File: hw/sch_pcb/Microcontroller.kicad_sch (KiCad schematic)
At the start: 32 parts

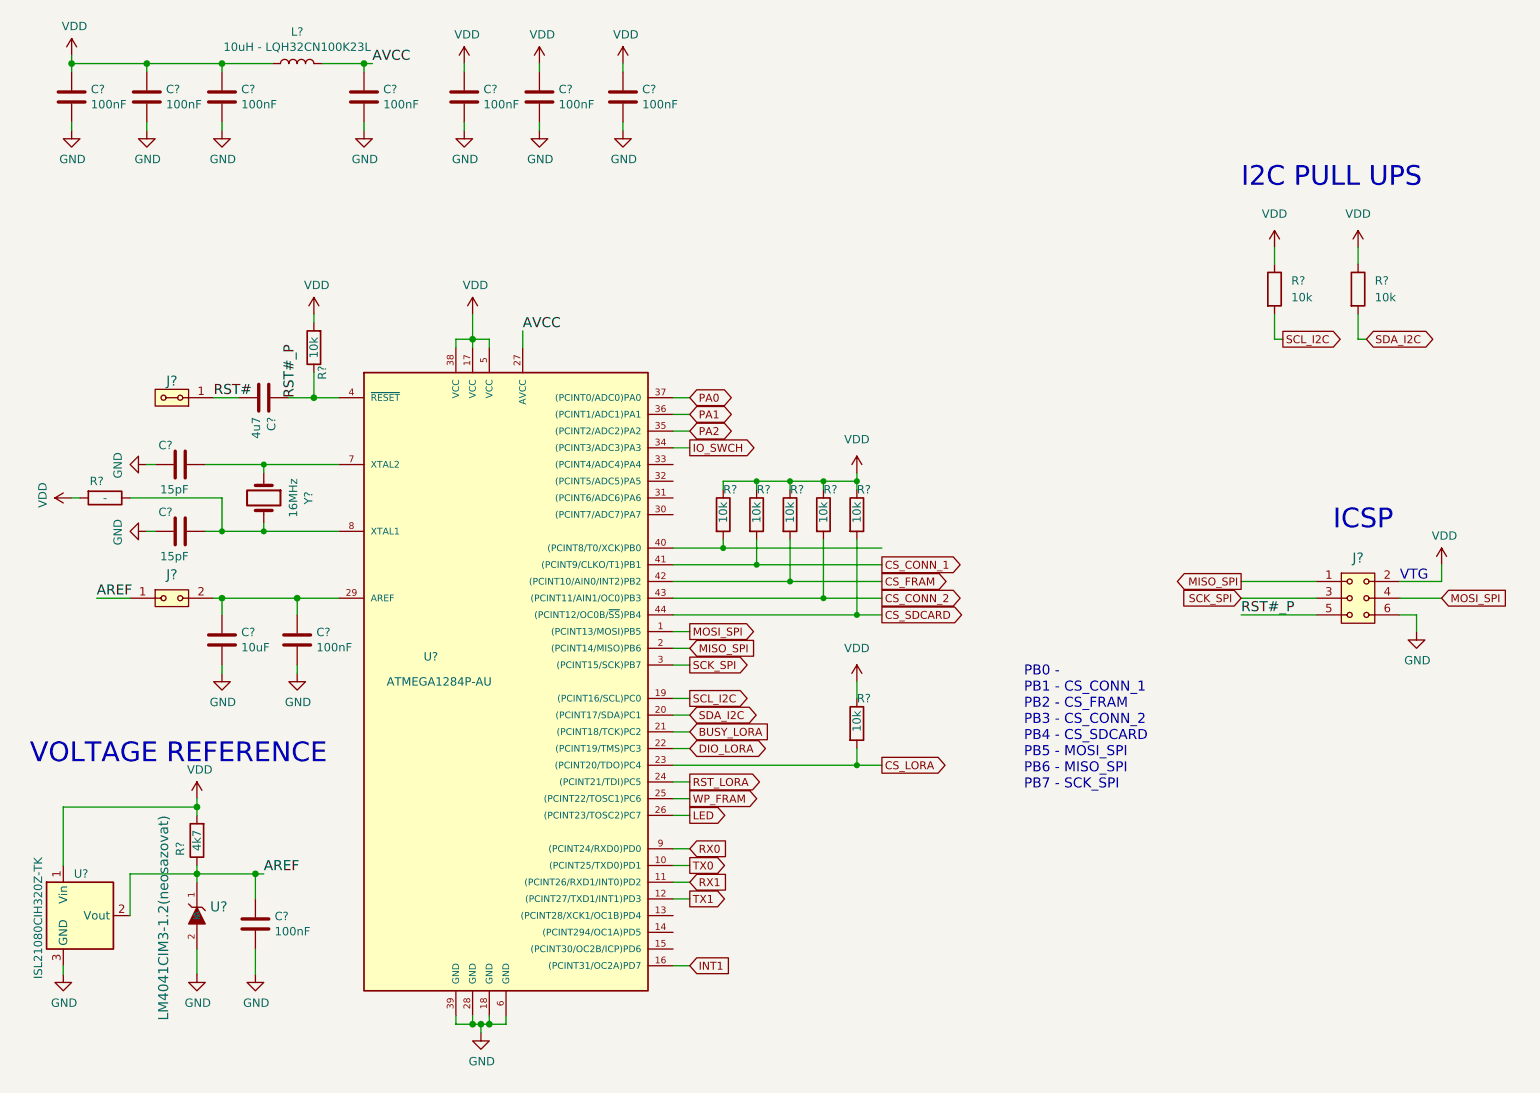
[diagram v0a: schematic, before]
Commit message: schematics update - LTC4041, TPS631000
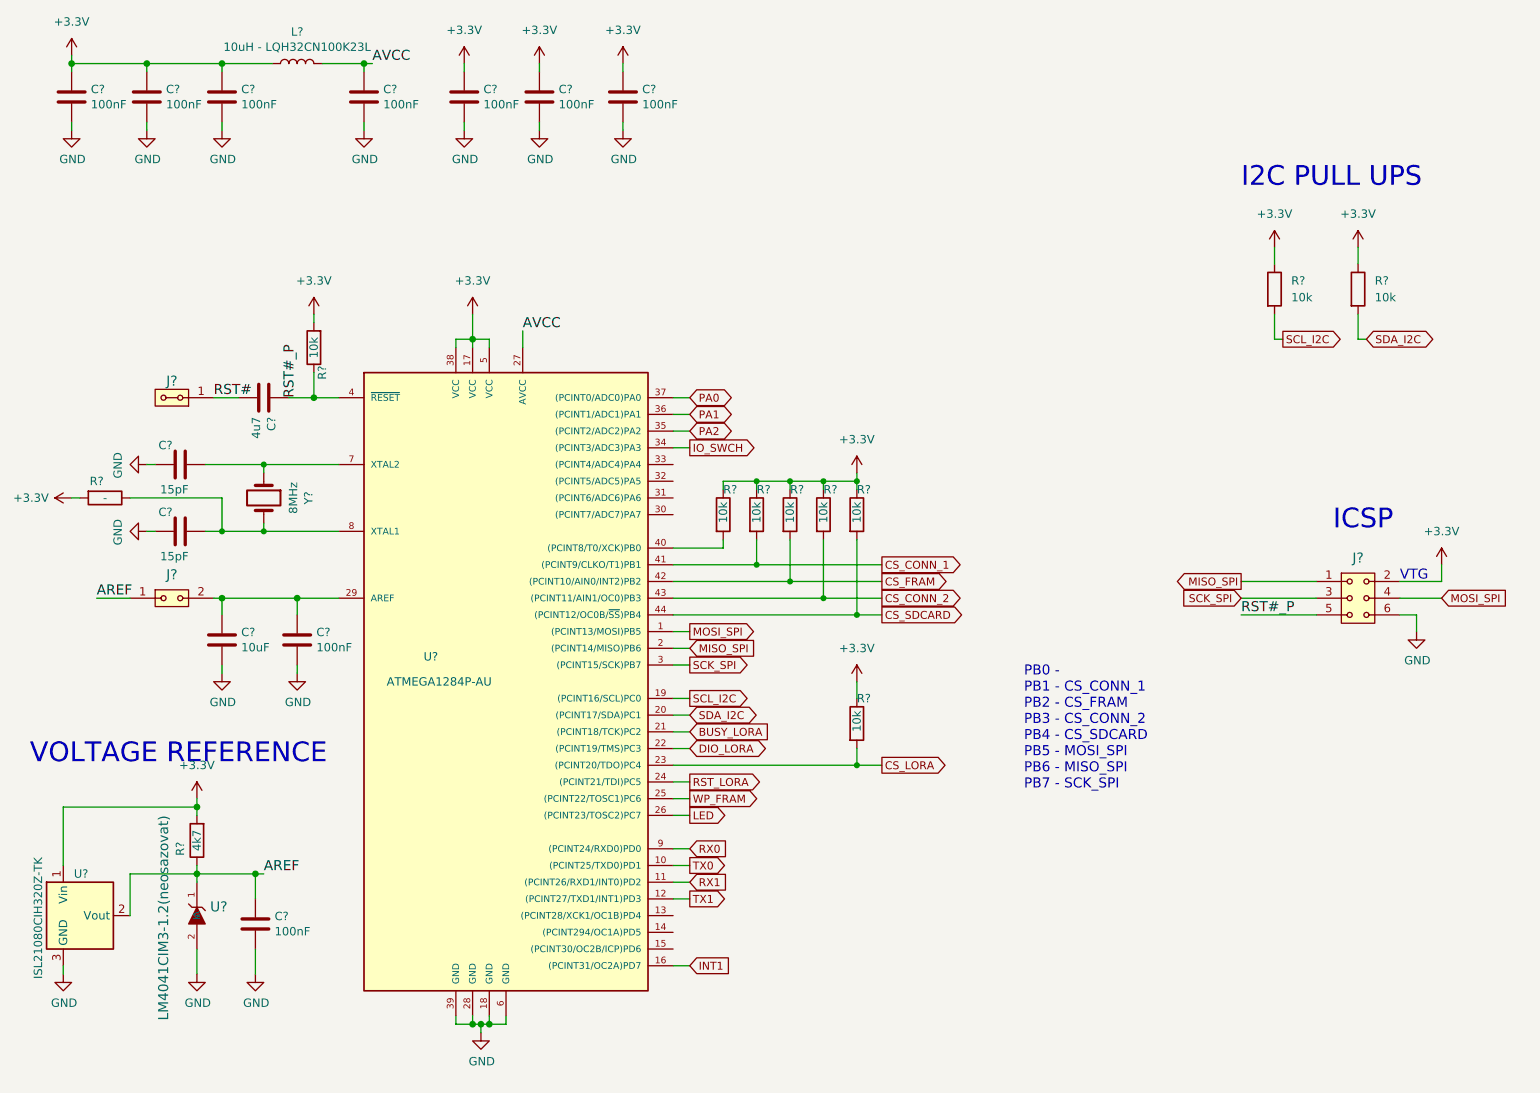
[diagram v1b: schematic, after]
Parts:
- Y?: value 16MHz -> 8MHz
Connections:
- net VDD renamed +3.3V
